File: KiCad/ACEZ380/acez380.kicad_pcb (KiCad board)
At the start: 2 copper layers, 160 x 160.8 mm, 146 parts, among them IC1 LM7805_TO220, J300 Conn_02x05_Odd_Even, J301 Conn_02x05_Odd_Even, J303 Conn_02x04_Odd_Even, J304 Conn_02x04_Odd_Even, J400 48409-0003, J402 Conn_02x06_Odd_Even, J501 Conn_02x05_Odd_Even, J502 Conn_02x03_Odd_Even, J503 Conn_02x05_Odd_Even, J604 Conn_02x03_Odd_Even, J605 Conn_02x03_Odd_Even, J607 Conn_02x04_Odd_Even, Q1 2N3904, Q100 2N3904, Q3 BC183, X1 CRYSTALHC49U-V 6.556MHz, X2 20MHz

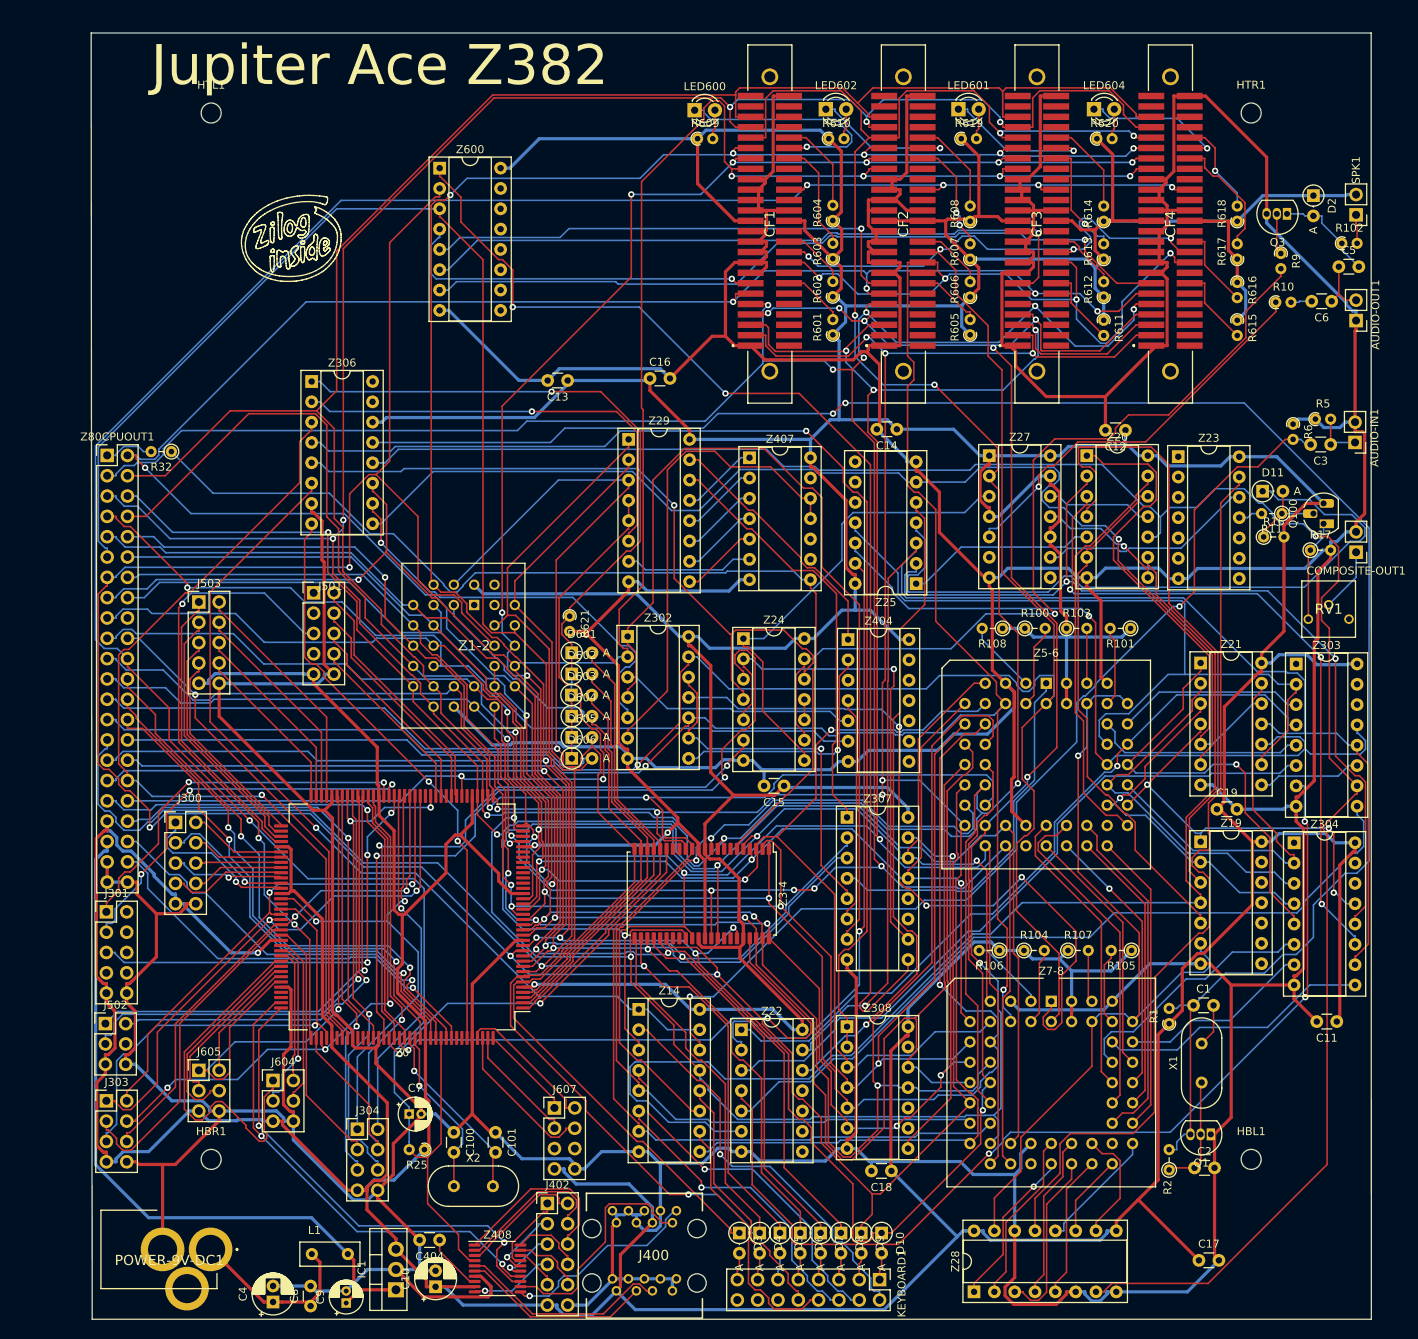
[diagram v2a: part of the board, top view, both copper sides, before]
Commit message: First complete system. Unlikely to work but will serve as the basis of a system to test VGA.
Signed-off-by: John Bradley <flypie@rocketmail.com>
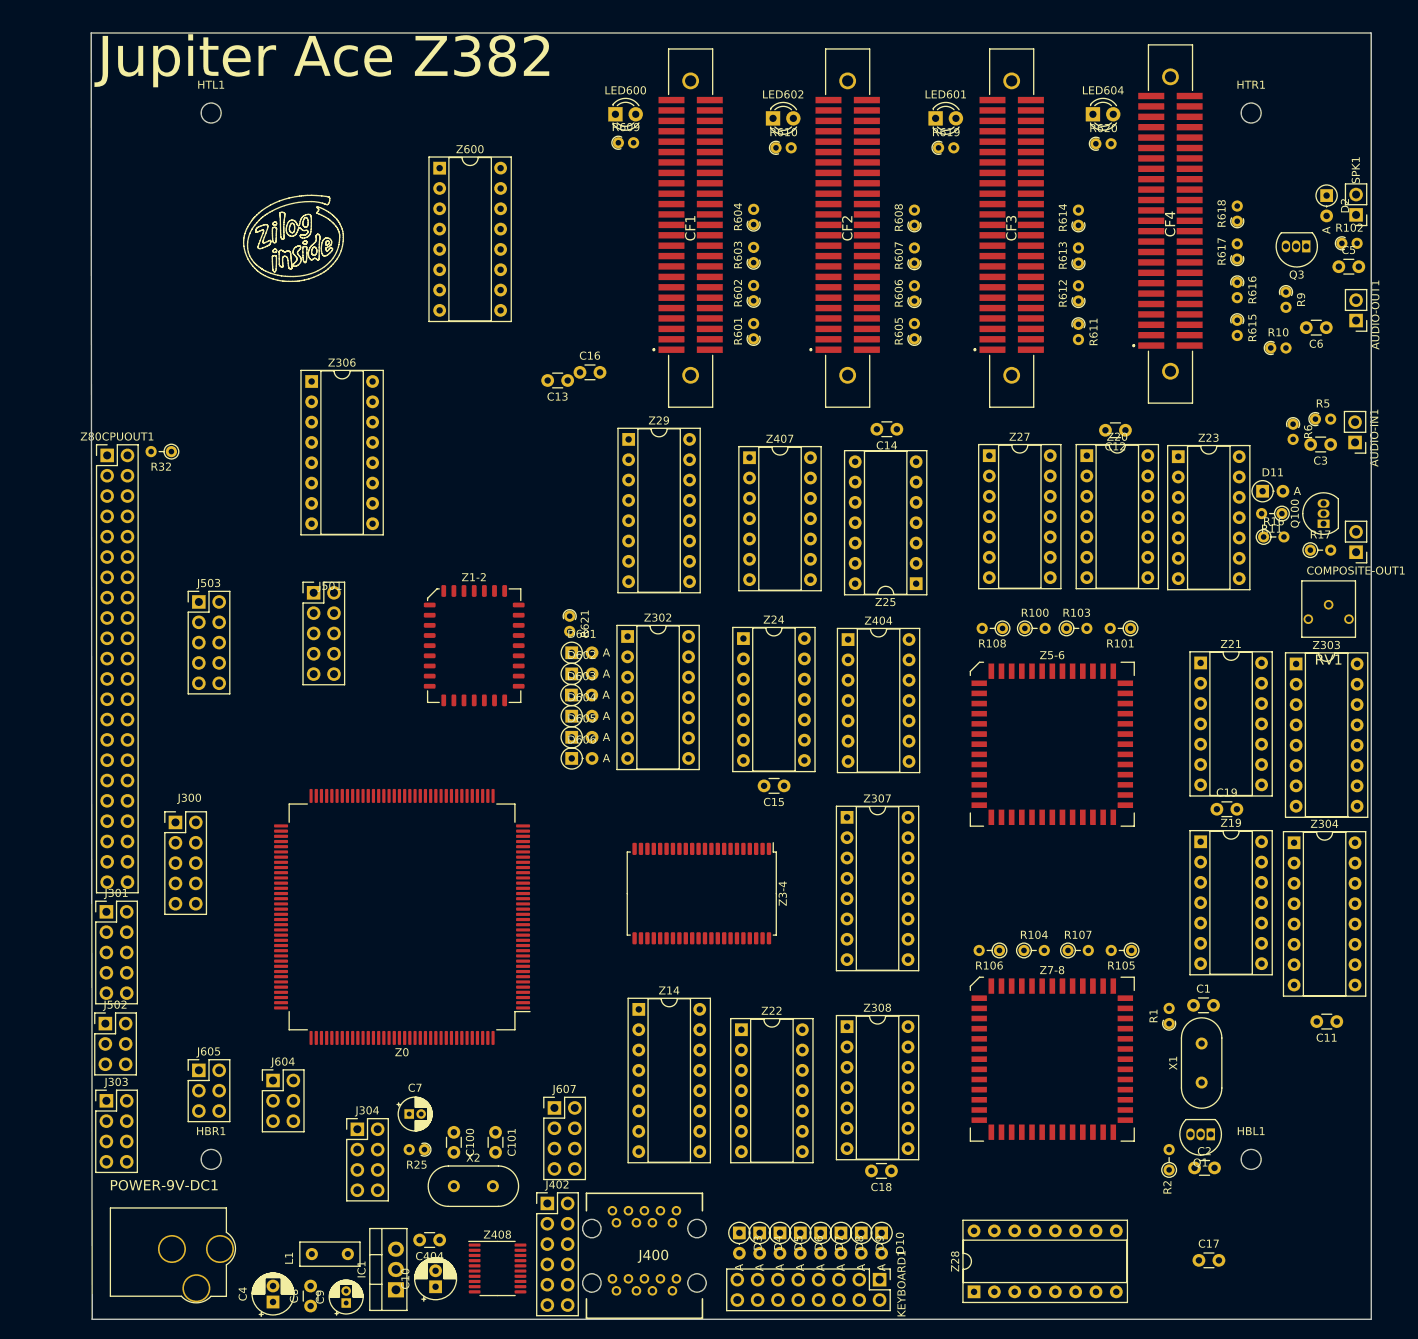
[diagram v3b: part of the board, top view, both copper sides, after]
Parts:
- J400: footprint SamacSys_Parts:48409-0003 -> ExtraFootprints:48409-0003
- L1: footprint SamacSys_Parts:KEMET_SBT_0260T -> ExtraFootprints:KEMET_SBT_0260T
- Logo1: footprint Symbol:ZilogInsideBack -> ExtraFootprints:ZilogInsideBack
- Logo2: footprint Symbol:ZilogInsideFront -> ExtraFootprints:ZilogInsideFront
- POWER-9V-DC1: footprint SamacSys_Parts:163179PHEX -> ExtraFootprints:163179PHEX
- Q1: footprint Package_TO_SOT_THT:TO-92L_Inline -> Package_TO_SOT_THT:TO-92_Inline
- Q100: footprint Package_TO_SOT_THT:TO-92L_HandSolder -> Package_TO_SOT_THT:TO-92_Inline
- RV1: footprint Potentiometer_THT:3362H1103LF -> ExtraFootprints:3362H1103LF
- Z1-2: footprint Package_LCC:PLCC-32_THT_Socket_11.4x14.0mm_P1.27mm -> Package_LCC:PLCC-32_11.4x14.0mm_P1.27mm
- Z5-6, Z7-8: footprint Package_LCC:PLCC-52_THT-Socket -> Package_LCC:PLCC-52
- moved R609 9.91 mm to (89.3, 36.6)
- moved CF1 9.91 mm to (98.3, 47.2)
- moved LED600 9.91 mm to (88.9, 33.0)
- moved R601 9.91 mm to (106.2, 61.1)
- moved R602 9.91 mm to (106.2, 56.3)
- moved R603 9.91 mm to (106.2, 51.6)
- moved R604 9.91 mm to (106.2, 46.8)
- moved C16 8.78 mm to (84.5, 65.3)
- moved POWER-9V-DC1 8.16 mm to (25.8, 179.8)
- moved Z5-6 7.66 mm to (143.5, 111.8)
- moved Z7-8 7.24 mm to (143.5, 151.1)
- moved CF2 6.99 mm to (117.9, 47.2)
- moved R605 6.99 mm to (126.3, 61.1)
- moved R606 6.99 mm to (126.3, 56.4)
- moved R607 6.99 mm to (126.3, 51.6)
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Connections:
- net /ADDRDECODE/~3C00-3FFF renamed /ADDRDECODE/~{3C00-3FFF}
- net /ADDRDECODE/~CPUFONT renamed /ADDRDECODE/~{CPUFONT}
- net /VDG/SH~LD renamed /VDG/SH~{LD}
- net /~BUSAK renamed /~{BUSAK}
- net /~BUSRQ renamed /~{BUSRQ}
- net /~HALT renamed /~{HALT}
- net /~WAIT renamed /~{WAIT}
- net /~WE renamed /~{WE}
- net RxS\~CTS renamed RxS\~{CTS}
- net ~0000-1FFF renamed ~{0000-1FFF}
- net ~3000-37FF renamed ~{3000-37FF}
- net ~3800-3BFF renamed ~{3800-3BFF}
- net ~3800-3FFF renamed ~{3800-3FFF}
- net ~CFCS renamed ~{CFCS}
- net ~CPUCLK renamed ~{CPUCLK}
- net ~CPUFONTRAM renamed ~{CPUFONTRAM}
- net ~CPUFONTROM renamed ~{CPUFONTROM}
- net ~CPUVIDEORAM renamed ~{CPUVIDEORAM}
- net ~CTS0 renamed ~{CTS0}
- net ~CTS1 renamed ~{CTS1}
- net ~DCD0 renamed ~{DCD0}
- net ~DCD1 renamed ~{DCD1}
- net ~INT0 renamed ~{INT0}
- net ~INT3 renamed ~{INT3}
- net ~IORD renamed ~{IORD}
- net ~IOREQ renamed ~{IOREQ}
- net ~IOWR renamed ~{IOWR}
- net ~M1 renamed ~{M1}
- net ~MRD renamed ~{MRD}
- net ~MREQ renamed ~{MREQ}
- net ~MWR renamed ~{MWR}
- net ~NMI renamed ~{NMI}
- net ~RAMSEL renamed ~{RAMSEL}
- net ~RD renamed ~{RD}
- net ~RESET renamed ~{RESET}
- net ~ROMSEL renamed ~{ROMSEL}
- net ~RTS0 renamed ~{RTS0}
- net ~RTS1 renamed ~{RTS1}
- net ~TAPECS renamed ~{TAPECS}
- net ~VIDEOCLK renamed ~{VIDEOCLK}
- net ~WR renamed ~{WR}
- CF1 pad 24: (no net) -> unconnected-(CF1-Pad24)
- CF1 pad 25: (no net) -> unconnected-(CF1-Pad25)
- CF1 pad 26: (no net) -> unconnected-(CF1-Pad26)
- CF1 pad 27: (no net) -> unconnected-(CF1-Pad27)
- CF1 pad 28: (no net) -> unconnected-(CF1-Pad28)
- CF1 pad 29: (no net) -> unconnected-(CF1-Pad29)
- CF1 pad 30: (no net) -> unconnected-(CF1-Pad30)
- CF1 pad 31: (no net) -> unconnected-(CF1-Pad31)
- CF1 pad 33: (no net) -> unconnected-(CF1-Pad33)
- CF1 pad 37: (no net) -> unconnected-(CF1-Pad37)
- CF1 pad 40: (no net) -> unconnected-(CF1-Pad40)
- CF1 pad 42: (no net) -> unconnected-(CF1-Pad42)
- CF1 pad 43: (no net) -> unconnected-(CF1-Pad43)
- CF1 pad 47: (no net) -> unconnected-(CF1-Pad47)
- CF1 pad 48: (no net) -> unconnected-(CF1-Pad48)
- CF1 pad 49: (no net) -> unconnected-(CF1-Pad49)
- CF2 pad 24: (no net) -> unconnected-(CF2-Pad24)
- CF2 pad 25: (no net) -> unconnected-(CF2-Pad25)
- CF2 pad 26: (no net) -> unconnected-(CF2-Pad26)
- CF2 pad 27: (no net) -> unconnected-(CF2-Pad27)
- CF2 pad 28: (no net) -> unconnected-(CF2-Pad28)
- CF2 pad 29: (no net) -> unconnected-(CF2-Pad29)
- CF2 pad 30: (no net) -> unconnected-(CF2-Pad30)
- CF2 pad 31: (no net) -> unconnected-(CF2-Pad31)
- CF2 pad 33: (no net) -> unconnected-(CF2-Pad33)
- CF2 pad 37: (no net) -> unconnected-(CF2-Pad37)
- CF2 pad 40: (no net) -> unconnected-(CF2-Pad40)
- CF2 pad 42: (no net) -> unconnected-(CF2-Pad42)
- CF2 pad 43: (no net) -> unconnected-(CF2-Pad43)
- CF2 pad 47: (no net) -> unconnected-(CF2-Pad47)
- CF2 pad 48: (no net) -> unconnected-(CF2-Pad48)
- CF2 pad 49: (no net) -> unconnected-(CF2-Pad49)
- CF3 pad 24: (no net) -> unconnected-(CF3-Pad24)
- CF3 pad 25: (no net) -> unconnected-(CF3-Pad25)
- CF3 pad 26: (no net) -> unconnected-(CF3-Pad26)
- CF3 pad 27: (no net) -> unconnected-(CF3-Pad27)
- CF3 pad 28: (no net) -> unconnected-(CF3-Pad28)
- CF3 pad 29: (no net) -> unconnected-(CF3-Pad29)
- CF3 pad 30: (no net) -> unconnected-(CF3-Pad30)
- CF3 pad 31: (no net) -> unconnected-(CF3-Pad31)
- CF3 pad 33: (no net) -> unconnected-(CF3-Pad33)
- CF3 pad 37: (no net) -> unconnected-(CF3-Pad37)
- CF3 pad 40: (no net) -> unconnected-(CF3-Pad40)
- CF3 pad 42: (no net) -> unconnected-(CF3-Pad42)
- CF3 pad 43: (no net) -> unconnected-(CF3-Pad43)
- CF3 pad 47: (no net) -> unconnected-(CF3-Pad47)
- CF3 pad 48: (no net) -> unconnected-(CF3-Pad48)
- CF3 pad 49: (no net) -> unconnected-(CF3-Pad49)
- CF4 pad 24: (no net) -> unconnected-(CF4-Pad24)
- CF4 pad 25: (no net) -> unconnected-(CF4-Pad25)
- CF4 pad 26: (no net) -> unconnected-(CF4-Pad26)
- CF4 pad 27: (no net) -> unconnected-(CF4-Pad27)
- CF4 pad 28: (no net) -> unconnected-(CF4-Pad28)
- CF4 pad 29: (no net) -> unconnected-(CF4-Pad29)
- CF4 pad 30: (no net) -> unconnected-(CF4-Pad30)
- CF4 pad 31: (no net) -> unconnected-(CF4-Pad31)
- CF4 pad 33: (no net) -> unconnected-(CF4-Pad33)
- CF4 pad 37: (no net) -> unconnected-(CF4-Pad37)
- CF4 pad 40: (no net) -> unconnected-(CF4-Pad40)
- CF4 pad 42: (no net) -> unconnected-(CF4-Pad42)
- CF4 pad 43: (no net) -> unconnected-(CF4-Pad43)
- CF4 pad 47: (no net) -> unconnected-(CF4-Pad47)
- CF4 pad 48: (no net) -> unconnected-(CF4-Pad48)
- CF4 pad 49: (no net) -> unconnected-(CF4-Pad49)
- J301 pad 2: (no net) -> unconnected-(J301-Pad2)
- J301 pad 4: (no net) -> unconnected-(J301-Pad4)
- J301 pad 6: (no net) -> unconnected-(J301-Pad6)
- J301 pad 7: (no net) -> unconnected-(J301-Pad7)
- J301 pad 8: (no net) -> unconnected-(J301-Pad8)
- J400 pad 10: GND -> +5V
- J400 pad 11: GND -> Net-(J400-Pad11)
- J400 pad 12: +5V -> Net-(J400-Pad12)
- J400 pad 13: Net-(J400-Pad13) -> GND
- J400 pad 14: Net-(J400-Pad14) -> GND
- J501 pad 1: (no net) -> unconnected-(J501-Pad1)
- J501 pad 3: (no net) -> unconnected-(J501-Pad3)
- J501 pad 7: (no net) -> unconnected-(J501-Pad7)
- J502 pad 4: (no net) -> unconnected-(J502-Pad4)
- J607 pad 5: (no net) -> unconnected-(J607-Pad5)
- J607 pad 6: (no net) -> unconnected-(J607-Pad6)
- KEYBOARD1 pad 12: (no net) -> unconnected-(KEYBOARD1-Pad12)
- KEYBOARD1 pad 14: (no net) -> unconnected-(KEYBOARD1-Pad14)
- KEYBOARD1 pad 16: (no net) -> unconnected-(KEYBOARD1-Pad16)
- POWER-9V-DC1 pad B: (no net) -> unconnected-(POWER-9V-DC1-PadB)
- RV1 pad 3: (no net) -> unconnected-(RV1-Pad3)
- Z0 pad 105: (no net) -> unconnected-(Z0-Pad105)
- Z0 pad 106: (no net) -> unconnected-(Z0-Pad106)
- Z0 pad 114: (no net) -> unconnected-(Z0-Pad114)
- Z0 pad 118: (no net) -> unconnected-(Z0-Pad118)
- Z0 pad 119: (no net) -> unconnected-(Z0-Pad119)
- Z0 pad 120: (no net) -> unconnected-(Z0-Pad120)
- Z0 pad 137: (no net) -> /~{INT1}
- Z0 pad 138: (no net) -> /~{INT2}
- Z0 pad 24: (no net) -> /DA15
- Z0 pad 25: (no net) -> /DA14
- Z0 pad 26: (no net) -> /DA13
- Z0 pad 27: (no net) -> /DA12
- Z0 pad 28: (no net) -> /DA11
- Z0 pad 29: (no net) -> /DA10
- Z0 pad 30: (no net) -> /DA9
- Z0 pad 31: (no net) -> /DA8
- Z0 pad 42: (no net) -> unconnected-(Z0-Pad42)
- Z0 pad 46: (no net) -> unconnected-(Z0-Pad46)
- Z0 pad 88: (no net) -> unconnected-(Z0-Pad88)
- Z1-2 pad 1: (no net) -> unconnected-(Z1-2-Pad1)
- Z1-2 pad 30: (no net) -> unconnected-(Z1-2-Pad30)
- Z1-2 pad 31: (no net) -> unconnected-(Z1-2-Pad31)
- Z27 pad 6: (no net) -> unconnected-(Z27-Pad6)
- Z27 pad 8: (no net) -> unconnected-(Z27-Pad8)
- Z3-4 pad 15: (no net) -> unconnected-(Z3-4-Pad15)
- Z3-4 pad 16: (no net) -> unconnected-(Z3-4-Pad16)
- Z3-4 pad 29: (no net) -> unconnected-(Z3-4-Pad29)
- Z3-4 pad 30: (no net) -> unconnected-(Z3-4-Pad30)
- Z3-4 pad 37: (no net) -> unconnected-(Z3-4-Pad37)
- Z3-4 pad 38: (no net) -> unconnected-(Z3-4-Pad38)
- Z3-4 pad 7: (no net) -> unconnected-(Z3-4-Pad7)
- Z3-4 pad 8: (no net) -> unconnected-(Z3-4-Pad8)
- Z303 pad 1: (no net) -> unconnected-(Z303-Pad1)
- Z303 pad 14: (no net) -> unconnected-(Z303-Pad14)
- Z303 pad 15: (no net) -> unconnected-(Z303-Pad15)
- Z304 pad 1: (no net) -> unconnected-(Z304-Pad1)
- Z304 pad 14: (no net) -> unconnected-(Z304-Pad14)
- Z304 pad 15: (no net) -> unconnected-(Z304-Pad15)
- Z307 pad 11: (no net) -> /~{IOREQ&11111101B}
- Z307 pad 12: (no net) -> /~{IOREQ&11111100B}
- Z408 pad 11: Net-(J400-Pad14) -> Net-(J400-Pad12)
- Z408 pad 12: Net-(J400-Pad13) -> Net-(J400-Pad11)
- Z5-6 pad 25: (no net) -> unconnected-(Z5-6-Pad25)
- Z5-6 pad 35: (no net) -> unconnected-(Z5-6-Pad35)
- Z600 pad 10: (no net) -> unconnected-(Z600-Pad10)
- Z600 pad 11: (no net) -> unconnected-(Z600-Pad11)
- Z600 pad 12: (no net) -> unconnected-(Z600-Pad12)
- Z600 pad 13: (no net) -> unconnected-(Z600-Pad13)
- Z600 pad 14: (no net) -> unconnected-(Z600-Pad14)
- Z600 pad 15: (no net) -> unconnected-(Z600-Pad15)
- Z600 pad 9: (no net) -> unconnected-(Z600-Pad9)
- Z7-8 pad 25: (no net) -> unconnected-(Z7-8-Pad25)
- Z7-8 pad 35: (no net) -> unconnected-(Z7-8-Pad35)
- Z80CPUOUT1 pad 18: (no net) -> /~{RFSH}
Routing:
- net GND: track 1378.5 -> 0.00 mm, vias 2 -> 0
- net +5V: track 1362.7 -> 0.00 mm, vias 2 -> 0
- net DA0: track 406.7 -> 0.00 mm, vias 9 -> 0
- net DA2: track 399.9 -> 0.00 mm, vias 2 -> 0
- net DA1: track 389.8 -> 0.00 mm, vias 8 -> 0
- net DA7: track 376.8 -> 0.00 mm, vias 8 -> 0
- net DA6: track 367.1 -> 0.00 mm, vias 11 -> 0
- net A12: track 353.6 -> 0.00 mm, vias 8 -> 0
- net DA4: track 351.2 -> 0.00 mm, vias 7 -> 0
- net DA5: track 348.1 -> 0.00 mm, vias 9 -> 0
- net A9: track 338.5 -> 0.00 mm, vias 4 -> 0
- net A10: track 336.5 -> 0.00 mm, vias 7 -> 0
- net A11: track 333.1 -> 0.00 mm, vias 10 -> 0
- net DA3: track 326.4 -> 0.00 mm, vias 7 -> 0
- net A8: track 317.3 -> 0.00 mm, vias 5 -> 0
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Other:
- net class Default removed
- net class Power removed
